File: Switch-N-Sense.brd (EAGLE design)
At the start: 80 x 50 mm, 40 parts, among them Q1 ZXMP10A13F, Q2 FDMT80080DC, Q3 FDMT80080DC, Q4 FDMT80080DC, Q5 FDMT80080DC, U1 BQ76200

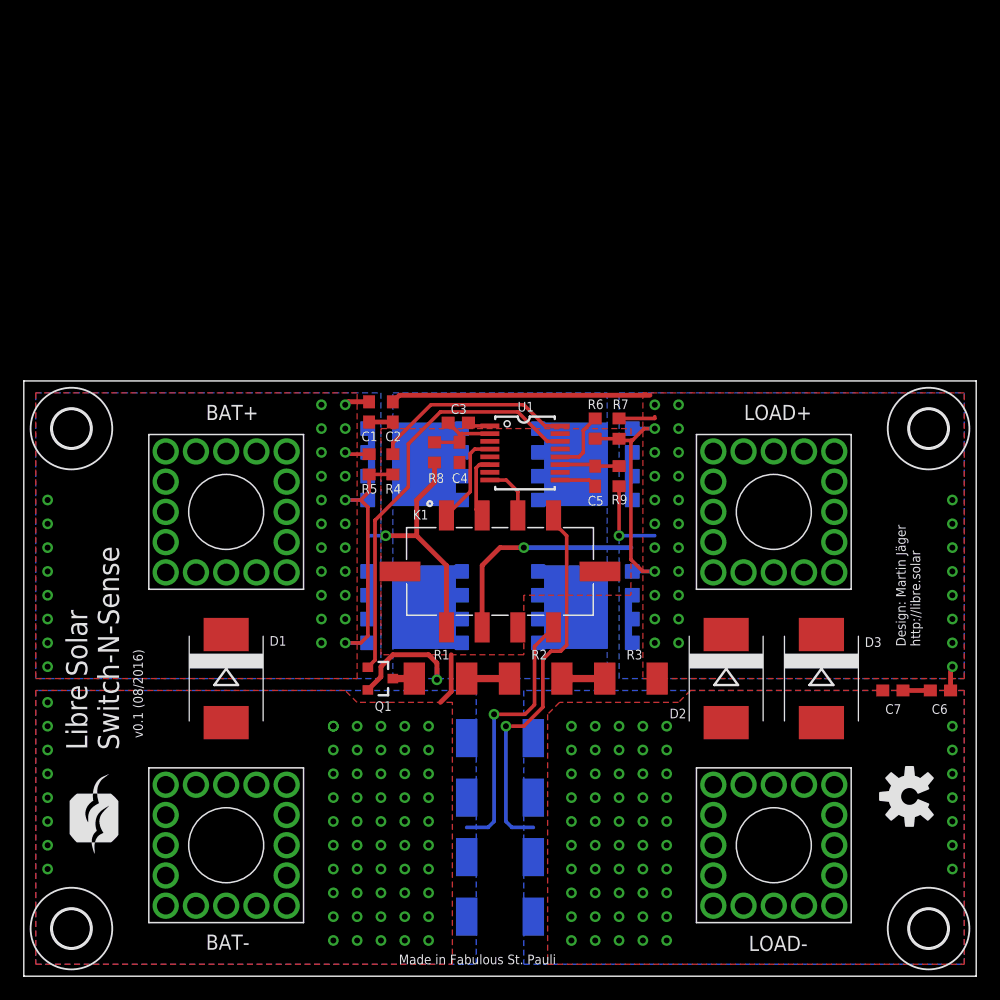
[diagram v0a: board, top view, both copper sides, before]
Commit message: Update to mate with new LibreSolar BMS48V
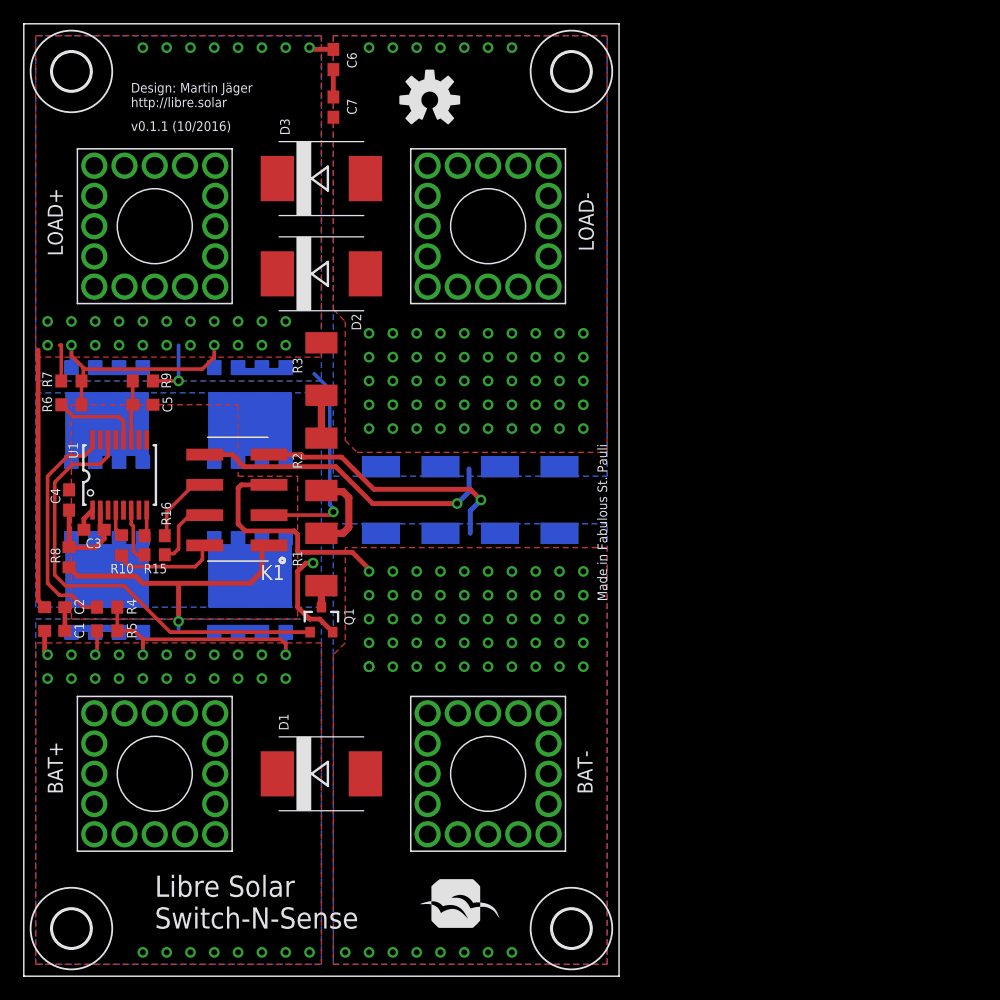
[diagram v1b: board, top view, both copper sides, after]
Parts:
- added R10, R15, R16: 1k, rcl:R0603
- C3: value 1µ -> 2.2µ
- K1: value (none) -> 61000821121; device Wire_to_Board_Connectors_rev15d:662008231822 -> Board_to_Board_Connectors_rev15d:61000821121
- moved H3 78.0 mm to (4.00, 76.0), turned to 90 degrees
- moved H4 78.0 mm to (46.0, 76.0), turned to 90 degrees
- moved C6 73.6 mm to (26.0, 77.0), turned to 270 degrees
- moved N1 71.0 mm to (34.1, 73.6), turned to 0 degrees
- moved C7 67.9 mm to (26.0, 73.0), turned to 270 degrees
- moved D3 59.4 mm to (25.0, 67.0), turned to 0 degrees
- moved LOAD+ 57.3 mm to (11.0, 63.0), turned to 90 degrees
- moved LOAD- 57.3 mm to (39.0, 63.0), turned to 90 degrees
- moved D2 48.1 mm to (25.0, 59.0), turned to 0 degrees
- moved R7 46.2 mm to (4.00, 50.0), turned to 180 degrees
- moved R6 44.0 mm to (4.00, 48.0), turned to 0 degrees
- moved Q3 42.4 mm to (7.00, 49.0), turned to 180 degrees
- moved H1 42.0 mm to (4.00, 4.00), turned to 90 degrees
- moved H2 42.0 mm to (46.0, 4.00), turned to 90 degrees
- moved R9 40.8 mm to (10.0, 50.0), turned to 0 degrees
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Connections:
- new net N$4: K1.7, R15.1
- new net N$5: K1.6, R16.1
- new net N$6: K1.8, R10.1
- net BAT+: now also K1.1; no longer K1.5
- net CHG_EN: now also R10.2; no longer K1.1
- net DSG_EN: now also R15.2; no longer K1.2
- net GND: now also K1.3, K1.4, U1.5, U1.7; no longer K1.7, K1.8
- net LOAD+: now also K1.2; no longer K1.6
- net LOAD-: now also K1.5; no longer K1.4
- net PCHG_EN: now also R16.2; no longer K1.3
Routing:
- net GND: track 29.9 -> 42.0 mm
- net N$6: track 0.00 -> 8.86 mm
- net N$5: track 0.00 -> 6.20 mm
- net N$4: track 0.00 -> 5.84 mm
- net LOAD-: track 32.1 -> 26.4 mm
- net CHG_EN: track 7.83 -> 2.30 mm
- net BAT+: track 23.6 -> 28.0 mm
- net N$2: track 3.60 -> 7.56 mm
- net PCHG: track 35.1 -> 38.0 mm
- net LOAD+: track 52.5 -> 50.0 mm
- net PCHG_EN: track 4.75 -> 2.22 mm
- net CHG: track 17.1 -> 19.4 mm
- net N$40: track 6.79 -> 8.92 mm
- net DSG: track 5.37 -> 7.37 mm
- net CHGDSG: track 10.2 -> 8.41 mm
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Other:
- board size 80 x 50 mm -> 50 x 80 mm
- board text added: "v0.1.1 (10/2016)"
- board text removed: "v0.1 (08/2016)"

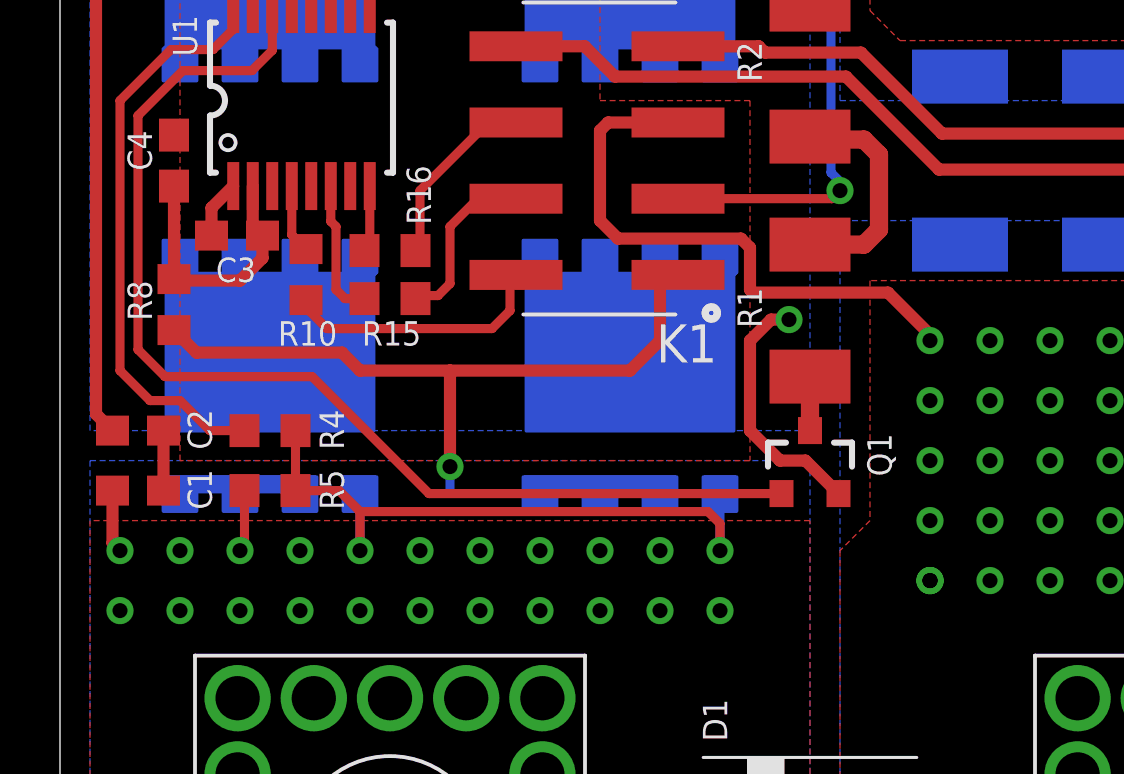
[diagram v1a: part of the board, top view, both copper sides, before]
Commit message: Updated board and schematic to fix issue #1
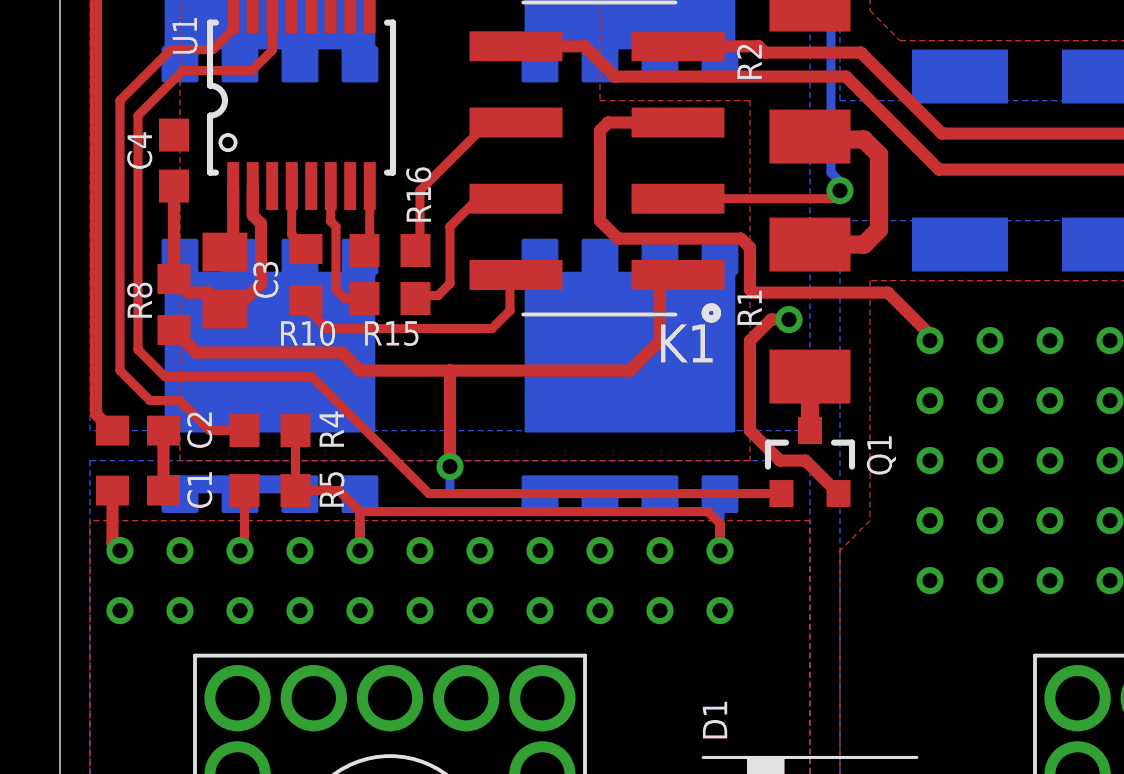
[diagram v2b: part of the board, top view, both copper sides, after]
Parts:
- C3: device rcl:C0603 -> rcl:C0805
- D1, D3: value SMCJ75A -> SMCJ60A
- R11, R12, R13, R14: value 1m -> 3m
- moved C3 1.55 mm to (5.50, 36.0), turned to 90 degrees
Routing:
- net N$40: track 8.92 -> 10.1 mm
- net GND: vias 60 -> 59
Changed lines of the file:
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@@
 <?xml version="1.0" encoding="utf-8"?>
 <!DOCTYPE eagle SYSTEM "eagle.dtd">
-<eagle version="7.6.0">
+<eagle version="7.7.0">
 <drawing>
 <settings>
@@
 <attribute name="VALUE" x="5.705" y="39.365" size="1.27" layer="27" rot="R90"/>
 </element>
-<element name="C3" library="rcl" package="C0603" value="2.2µ" x="5.9" y="37.5" smashed="yes" rot="R180">
-<attribute name="MPN" value="0603B104K500CT" x="5.9" y="37.5" size="1.778" layer="27" rot="R180" display="off"/>
-<attribute name="OC_FARNELL" value="2496834" x="5.9" y="37.5" size="1.778" layer="27" rot="R180" display="off"/>
-<attribute name="MF" value="WALSIN" x="5.9" y="37.5" size="1.778" layer="27" rot="R180" display="off"/>
-<attribute name="NAME" x="6.535" y="36.765" size="0.8128" layer="25" rot="R180"/>
-<attribute name="VALUE" x="6.535" y="39.405" size="1.27" layer="27" rot="R180"/>
+<element name="C3" library="rcl" package="C0805" value="2.2µ" x="5.5" y="36" smashed="yes" rot="R90">
+<attribute name="MPN" value="0603B104K500CT" x="5.5" y="36" size="1.778" layer="27" rot="R90" display="off"/>
+<attribute name="OC_FARNELL" value="2496834" x="5.5" y="36" size="1.778" layer="27" rot="R90" display="off"/>
+<attribute name="MF" value="WALSIN" x="5.5" y="36" size="1.778" layer="27" rot="R90" display="off"/>
+<attribute name="NAME" x="7.265" y="35.365" size="0.8128" layer="25" rot="R90"/>
+<attribute name="VALUE" x="7.405" y="35.365" size="1.27" layer="27" rot="R90"/>
 </element>
 <element name="R9" library="rcl" package="R0603" value="100" x="10" y="50" smashed="yes">
@@
 <attribute name="VALUE" x="47.89" y="59.19" size="1.27" layer="27" rot="R90"/>
 </element>
-<element name="R11" library="rcl" package="R2512" value="1m" x="30" y="40" smashed="yes" rot="MR90">
+<element name="R11" library="rcl" package="R2512" value="3m" x="30" y="40" smashed="yes" rot="MR90">
 <attribute name="MPN" value="" x="30" y="40" size="1.778" layer="28" rot="MR90" display="off"/>
 <attribute name="OC_FARNELL" value="unknown" x="30" y="40" size="1.778" layer="28" rot="MR90" display="off"/>
@@
 <attribute name="VALUE" x="26.825" y="37.46" size="1.27" layer="28" rot="MR90"/>
 </element>
-<element name="R12" library="rcl" package="R2512" value="1m" x="35" y="40" smashed="yes" rot="MR90">
+<element name="R12" library="rcl" package="R2512" value="3m" x="35" y="40" smashed="yes" rot="MR90">
 <attribute name="MPN" value="" x="35" y="40" size="1.778" layer="28" rot="MR90" display="off"/>
 <attribute name="OC_FARNELL" value="unknown" x="35" y="40" size="1.778" layer="28" rot="MR90" display="off"/>
@@
 <attribute name="VALUE" x="31.825" y="37.46" size="1.27" layer="28" rot="MR90"/>
 </element>
-<element name="R13" library="rcl" package="R2512" value="1m" x="40" y="40" smashed="yes" rot="MR90">
+<element name="R13" library="rcl" package="R2512" value="3m" x="40" y="40" smashed="yes" rot="MR90">
 <attribute name="MPN" value="" x="40" y="40" size="1.778" layer="28" rot="MR90" display="off"/>
 <attribute name="OC_FARNELL" value="unknown" x="40" y="40" size="1.778" layer="28" rot="MR90" display="off"/>
@@
 <attribute name="VALUE" x="36.825" y="37.46" size="1.27" layer="28" rot="MR90"/>
 </element>
-<element name="R14" library="rcl" package="R2512" value="1m" x="45" y="40" smashed="yes" rot="MR90">
+<element name="R14" library="rcl" package="R2512" value="3m" x="45" y="40" smashed="yes" rot="MR90">
 <attribute name="MPN" value="" x="45" y="40" size="1.778" layer="28" rot="MR90" display="off"/>
 <attribute name="OC_FARNELL" value="unknown" x="45" y="40" size="1.778" layer="28" rot="MR90" display="off"/>
@@
 <attribute name="VALUE" x="41.825" y="37.46" size="1.27" layer="28" rot="MR90"/>
 </element>
-<element name="D1" library="diode" package="SMC" value="SMCJ75A" x="25" y="17" smashed="yes">
+<element name="D1" library="diode" package="SMC" value="SMCJ60A" x="25" y="17" smashed="yes">
 <attribute name="MPN" value="SMCJ75A" x="25" y="17" size="1.778" layer="27" display="off"/>
 <attribute name="OC_FARNELL" value="2322496" x="25" y="17" size="1.778" layer="27" display="off"/>
@@
 <attribute name="VALUE" x="21.541" y="54.371" size="1.27" layer="27"/>
 </element>
-<element name="D3" library="diode" package="SMC" value="SMCJ75A" x="25" y="67" smashed="yes">
+<element name="D3" library="diode" package="SMC" value="SMCJ60A" x="25" y="67" smashed="yes">
 <attribute name="MPN" value="SMCJ75A" x="25" y="67" size="1.778" layer="27" display="off"/>
 <attribute name="OC_FARNELL" value="2322496" x="25" y="67" size="1.778" layer="27" display="off"/>
@@
 <via x="39" y="2" extent="1-16" drill="0.5"/>
 <via x="41" y="2" extent="1-16" drill="0.5"/>
-<via x="29" y="26" extent="1-16" drill="0.5"/>
 <via x="29" y="26" extent="1-16" drill="0.5"/>
 <via x="29" y="28" extent="1-16" drill="0.5"/>
@@
 <contactref element="U1" pad="1"/>
 <contactref element="C3" pad="2"/>
-<wire x1="5.05" y1="37.5" x2="5.05" y2="38.425" width="0.4064" layer="1"/>
-<wire x1="5.05" y1="38.425" x2="5.775" y2="39.15" width="0.4064" layer="1"/>
+<wire x1="5.775" y1="39.15" x2="5.775" y2="37.325" width="0.4064" layer="1"/>
+<wire x1="5.775" y1="37.325" x2="5.5" y2="36.95" width="0.4064" layer="1"/>
 </signal>
 <signal name="N$40">
@@
 <contactref element="R8" pad="1"/>
 <wire x1="3.8" y1="39.15" x2="3.8" y2="36.05" width="0.4064" layer="1"/>
-<wire x1="6.75" y1="37.5" x2="6.75" y2="36.75" width="0.4064" layer="1"/>
-<wire x1="6.75" y1="36.75" x2="6" y2="36" width="0.4064" layer="1"/>
-<wire x1="6" y1="36" x2="3.85" y2="36" width="0.4064" layer="1"/>
-<wire x1="3.85" y1="36" x2="3.8" y2="36.05" width="0.4064" layer="1"/>
-<wire x1="6.75" y1="37.5" x2="6.425" y2="37.825" width="0.4064" layer="1"/>
-<wire x1="6.425" y1="37.825" x2="6.425" y2="39.15" width="0.4064" layer="1"/>
+<wire x1="6.425" y1="39.15" x2="6.425" y2="38.175" width="0.4064" layer="1"/>
+<wire x1="6.425" y1="38.175" x2="6.7" y2="37.9" width="0.4064" layer="1"/>
+<wire x1="6.7" y1="37.9" x2="6.7" y2="35.9" width="0.4064" layer="1"/>
+<wire x1="6.7" y1="35.9" x2="6" y2="35.2" width="0.4064" layer="1"/>
+<wire x1="6" y1="35.2" x2="5.55" y2="35.1" width="0.4064" layer="1"/>
+<wire x1="5.55" y1="35.1" x2="5.5" y2="35.05" width="0.4064" layer="1"/>
+<wire x1="3.8" y1="36.05" x2="3.85" y2="36.05" width="0.4064" layer="1"/>
+<wire x1="3.85" y1="36.05" x2="4.3" y2="35.6" width="0.4064" layer="1"/>
+<wire x1="4.3" y1="35.6" x2="4.95" y2="35.6" width="0.4064" layer="1"/>
+<wire x1="4.95" y1="35.6" x2="5.5" y2="35.05" width="0.4064" layer="1"/>
 </signal>
 <signal name="N$41">
